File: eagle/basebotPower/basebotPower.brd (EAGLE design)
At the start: 30.1 x 26.7 mm, 7 parts

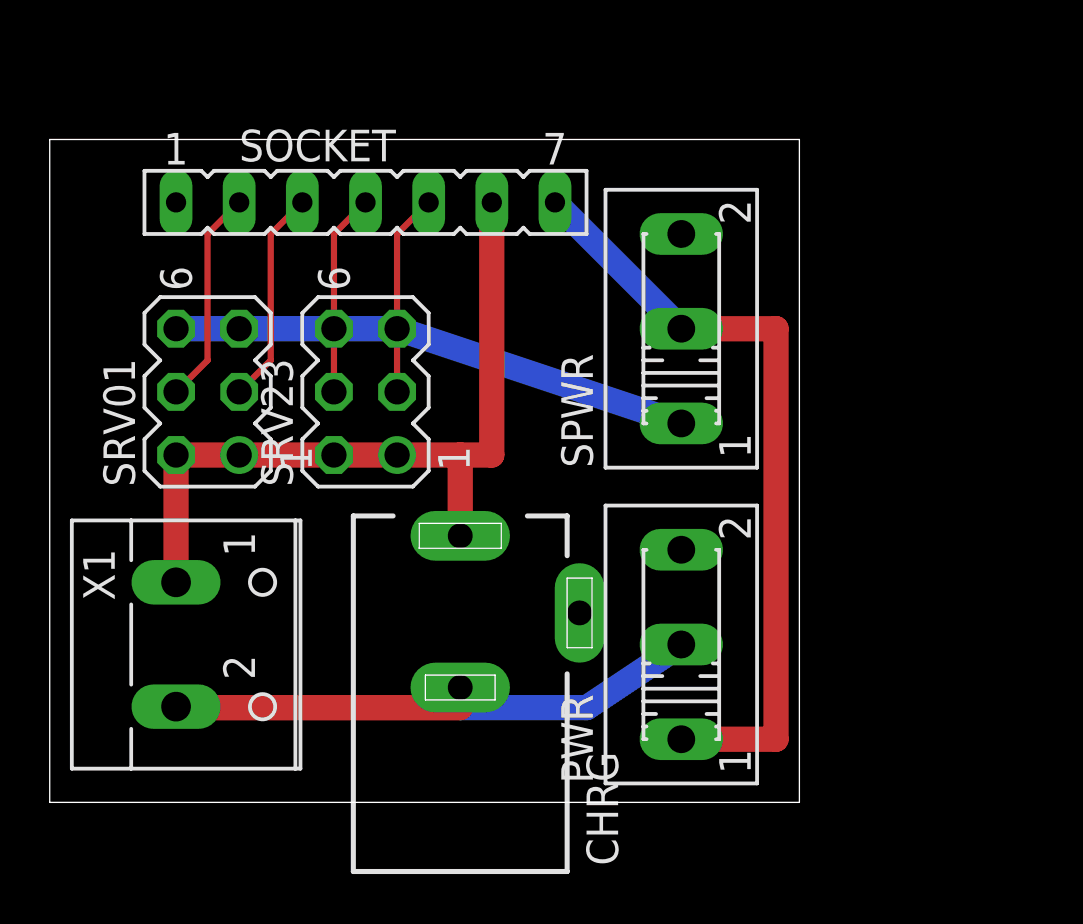
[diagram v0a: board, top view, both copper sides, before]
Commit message: Fixed stupid error in board involving the wrong wiring for the servos, also changed the layout to use screw terminals rather than on board switches, this allows for panel mount (and higher current) switches and means the board itself can be tucked away somewhere.
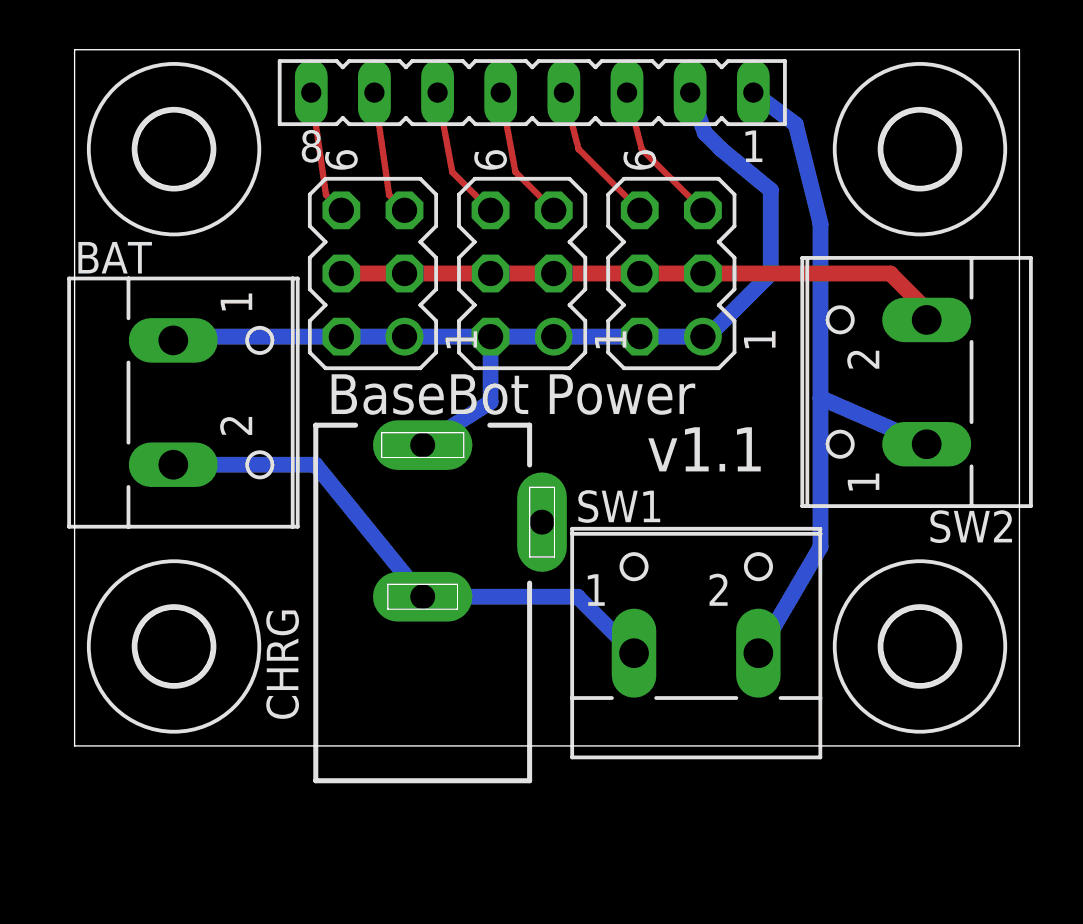
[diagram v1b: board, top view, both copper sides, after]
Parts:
- removed PWR, SPWR: (no value), switch:255SB
- removed SOCKET: (no value), con-lsta:FE07
- removed X1: (no value), con-wago-500:W237-102
- added BAT, SW1, SW2: (no value), con-wago-500:W237-102
- added SRV45: (no value), con-lstb:MA03-2
- added SV1: (no value), con-lsta:FE08
- added U$1, U$2, U$3, U$4: (no value), holes:3,0
- moved SRV01 13.5 mm to (19.0, 20.0)
- moved SRV23 4.77 mm to (13.0, 20.0)
- moved CHRG 3.95 mm to (15.0, 10.0)
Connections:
- new net N$12: SRV01.3, SRV01.4, SRV23.3, SRV23.4, SRV45.3, SRV45.4, SW2.2
- new net N$4: SRV23.5, SV1.7
- net GND: now also BAT.1, SRV45.1, SRV45.2, SV1.2; no longer SOCKET.6, X1.1
- net N$2: now also BAT.2, SW1.1; no longer PWR.2, X1.2
- net N$3: now also SV1.8; no longer SPWR.1, SRV01.5, SRV01.6, SRV23.5
- net N$5: now also SRV45.6, SV1.4; no longer SOCKET.5, SRV23.3
- net N$6: now also SRV45.5, SV1.3; no longer SOCKET.4, SRV23.4
- net N$7: now also SRV01.6, SV1.6; no longer SOCKET.3, SRV01.3
- net N$9: now also SRV01.5, SV1.5; no longer SOCKET.2, SRV01.4
- net SERVOPWR: now also SV1.1, SW1.2, SW2.1; no longer PWR.1, SOCKET.7, SPWR.2
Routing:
- net N$12: track 0.00 -> 24.6 mm
- net N$3: track 20.9 -> 5.04 mm
- net GND: track 31.2 -> 39.6 mm
- net N$4: track 0.00 -> 5.04 mm
- net N$9: track 8.67 -> 5.43 mm
- net N$7: track 8.67 -> 5.43 mm
- net SERVOPWR: track 31.3 -> 28.9 mm
- net N$6: track 8.15 -> 5.83 mm
- net N$5: track 8.15 -> 5.83 mm
- net N$2: track 22.7 -> 22.0 mm
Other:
- board size 30.1 x 26.7 mm -> 38 x 28 mm
- board text added: "+"
- board text added: "+VE"
- board text added: "-"
- board text added: "0"
- board text added: "1"
- board text added: "12 Jun '14"
- board text added: "2"
- board text added: "3"
- board text added: "4"
- board text added: "5"
- board text added: "BaseBot Power"
- board text added: "GND"
- board text added: "v1.1"
